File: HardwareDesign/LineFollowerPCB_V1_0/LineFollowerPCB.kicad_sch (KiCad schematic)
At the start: 16 parts, among them J1 B2B-XH-A, J2 B4B-XH-A, J3 Conn_01x04, J4 Conn_01x02_Socket, M1 Motor_DC, M2 Motor_DC, U1 Black Pill v2, U2 DRV8833, U3 AMS1117-3.3, U4 SX1308

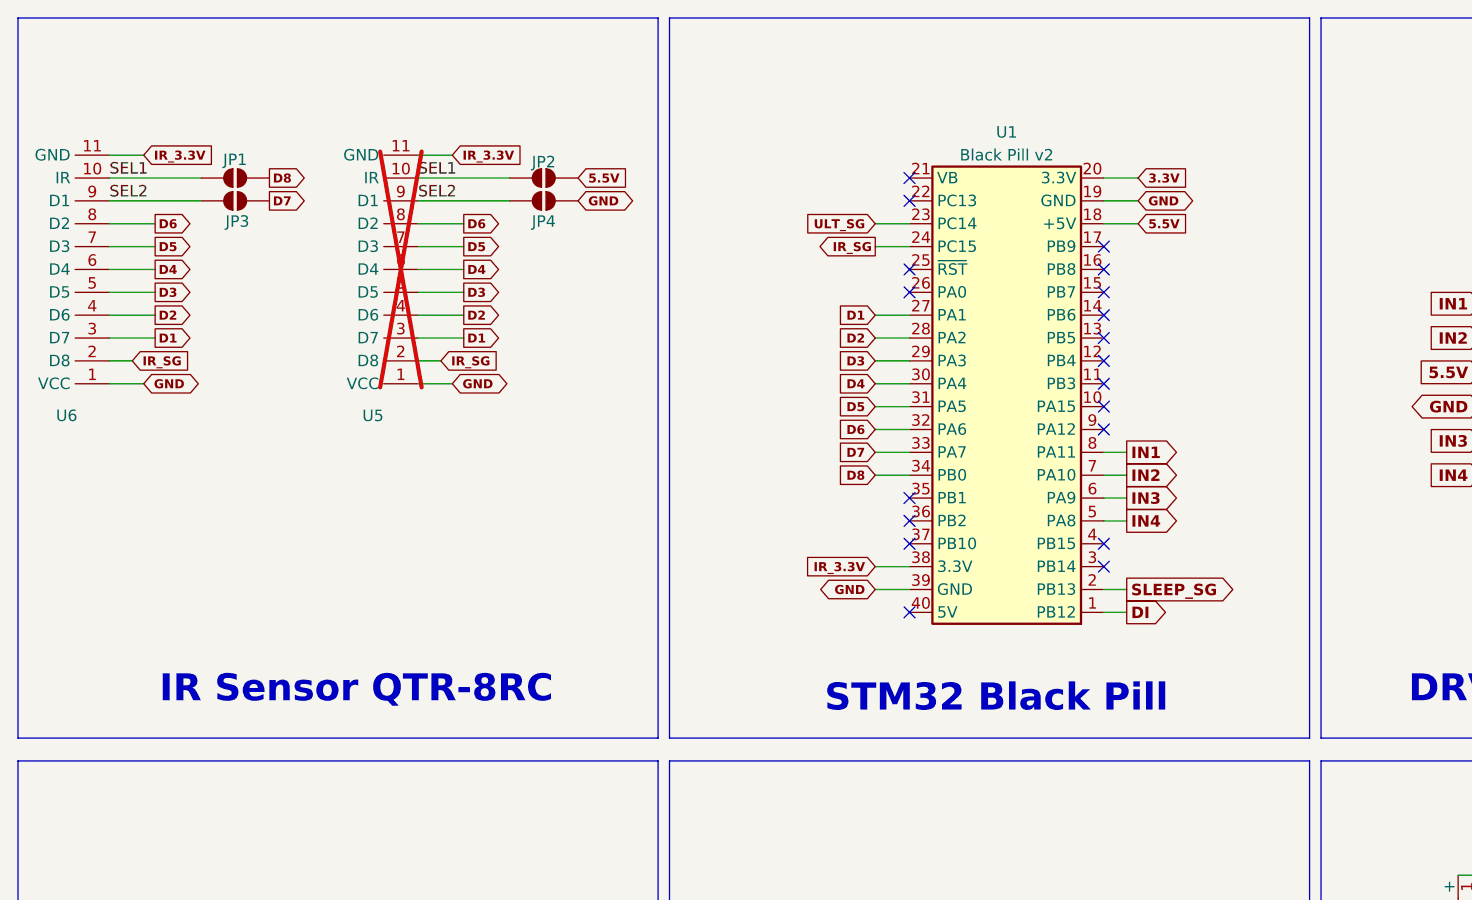
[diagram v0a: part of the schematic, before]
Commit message: Add 1N4001 doide and connect the 5V power signal to the sensor
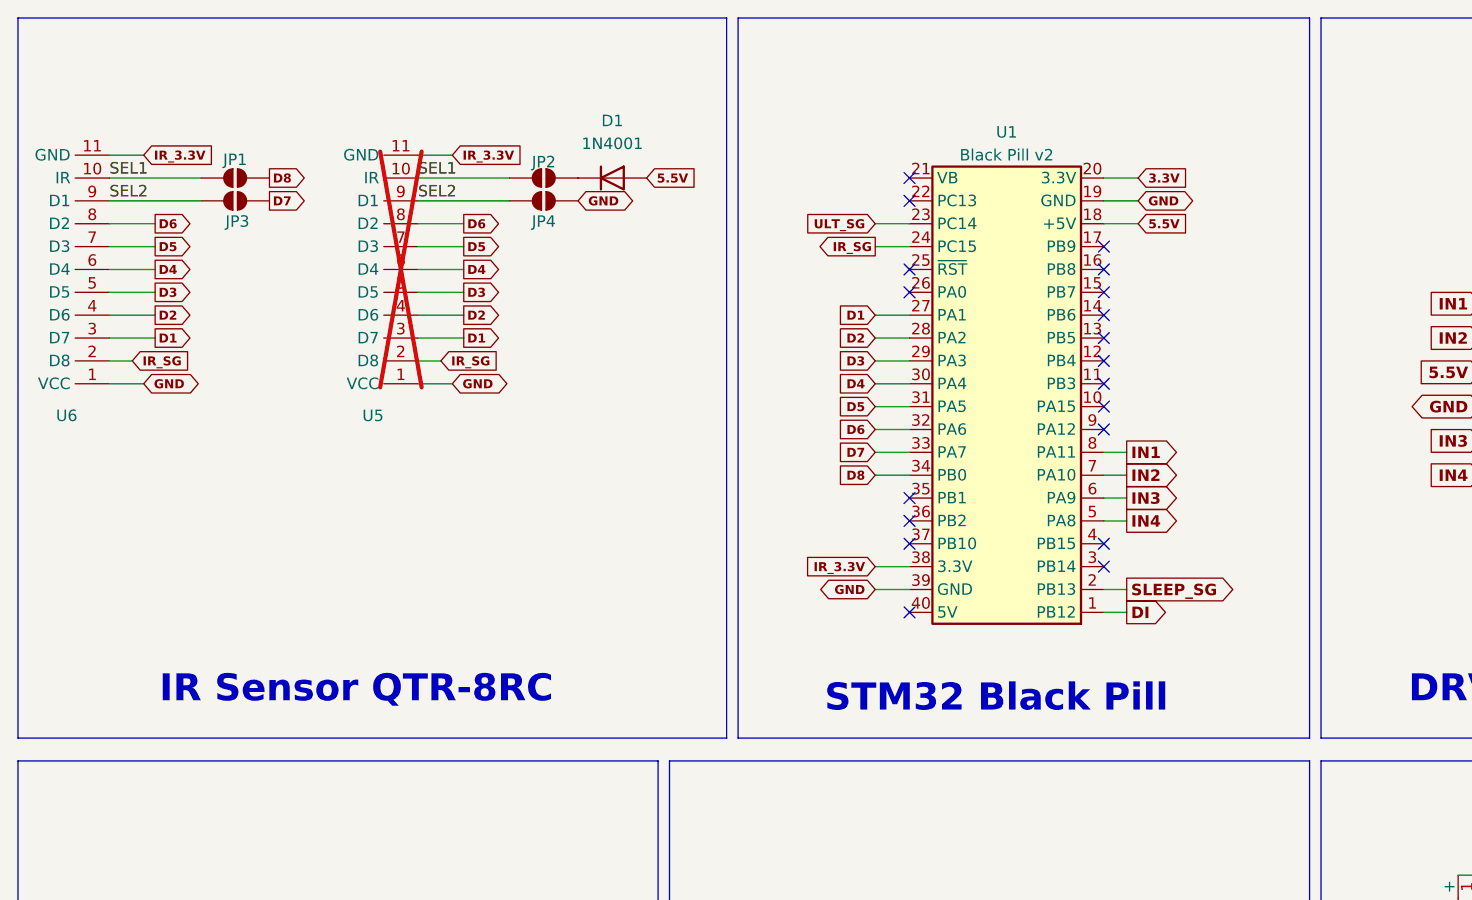
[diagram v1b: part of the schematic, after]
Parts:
- added D1: 1N4001, Diode_THT:D_DO-41_SOD81_P10.16mm_Horizontal, symbol Diode:1N4001
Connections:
- net 5.5V: now also D1.2 (A); no longer JP2.1 (A)
- new net: D1.1 (K), JP2.1 (A)
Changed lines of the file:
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@@
 	)
 	(rectangle
-		(start 85.09 12.7)
+		(start 92.71 12.7)
 		(end 156.21 92.71)
 		(stroke
@@
 	(rectangle
 		(start 12.7 12.7)
-		(end 83.82 92.71)
+		(end 91.44 92.71)
 		(stroke
 			(width 0)
@@
 		)
 	)
+	(global_label "5.5V"
+		(shape input)
+		(at 82.55 30.48 0)
+		(fields_autoplaced yes)
+		(effects
+			(font
+				(size 1 1)
+				(thickness 0.254)
+				(bold yes)
+			)
+			(justify left)
+		)
+		(property "Intersheetrefs" "${INTERSHEET_REFS}"
+			(at 88.7634 30.48 0)
+			(effects
+				(font
+					(size 1.27 1.27)
+				)
+				(justify left)
+				(hide yes)
+			)
+		)
+	)
 	(global_label "GND"
 		(shape bidirectional)
@@
 		)
 	)
-	(global_label "5.5V"
-		(shape input)
-		(at 74.93 30.48 0)
-		(fields_autoplaced yes)
-		(effects
-			(font
-				(size 1 1)
-				(thickness 0.254)
-				(bold yes)
-			)
-			(justify left)
-		)
-		(property "Intersheetrefs" "${INTERSHEET_REFS}"
-			(at 81.1434 30.48 0)
-			(effects
-				(font
-					(size 1.27 1.27)
-				)
-				(justify left)
-				(hide yes)
-			)
-		)
-	)
 	(global_label "OUT1"
 		(shape output)
@@
 					(unit 1)
 				)
+			)
+		)
+	)
+	(symbol
+		(lib_id "Diode:1N4001")
+		(at 78.74 30.48 0)
+		(unit 1)
+		(exclude_from_sim no)
+		(in_bom yes)
+		(on_board yes)
+		(dnp no)
+		(fields_autoplaced yes)
+		(property "Reference" "D1"
+			(at 78.74 24.13 0)
+			(effects
+				(font
+					(size 1.27 1.27)
+				)
+			)
+		)
+		(property "Value" "1N4001"
+			(at 78.74 26.67 0)
+			(effects
+				(font
+					(size 1.27 1.27)
+				)
+			)
+		)
+		(property "Footprint" "Diode_THT:D_DO-41_SOD81_P10.16mm_Horizontal"
+			(at 78.74 30.48 0)
+			(effects
+				(font
+					(size 1.27 1.27)
+				)
+				(hide yes)
+			)
+		)
+		(property "Datasheet" "http://www.vishay.com/docs/88503/1n4001.pdf"
+			(at 78.74 30.48 0)
+			(effects
+				(font
+					(size 1.27 1.27)
+				)
+				(hide yes)
+			)
+		)
+		(property "Description" "50V 1A General Purpose Rectifier Diode, DO-41"
+			(at 78.74 30.48 0)
+			(effects
+				(font
+					(size 1.27 1.27)
+				)
+				(hide yes)
+			)
+		)
+		(property "Sim.Device" "D"
+			(at 78.74 30.48 0)
+			(effects
+				(font
+					(size 1.27 1.27)
+				)
+				(hide yes)
+			)
+		)
+		(property "Sim.Pins" "1=K 2=A"
+			(at 78.74 30.48 0)
+			(effects
+				(font
+					(size 1.27 1.27)
+				)
+				(hide yes)
+			)
+		)
+		(pin "1"
+		)
+		(pin "2"
+		)
+		(instances
+			(project ""
+				(path "/d5afd7c7-15af-4d30-9f5b-830a3ba068cd"
+					(reference "D1")
+					(unit 1)
+				)

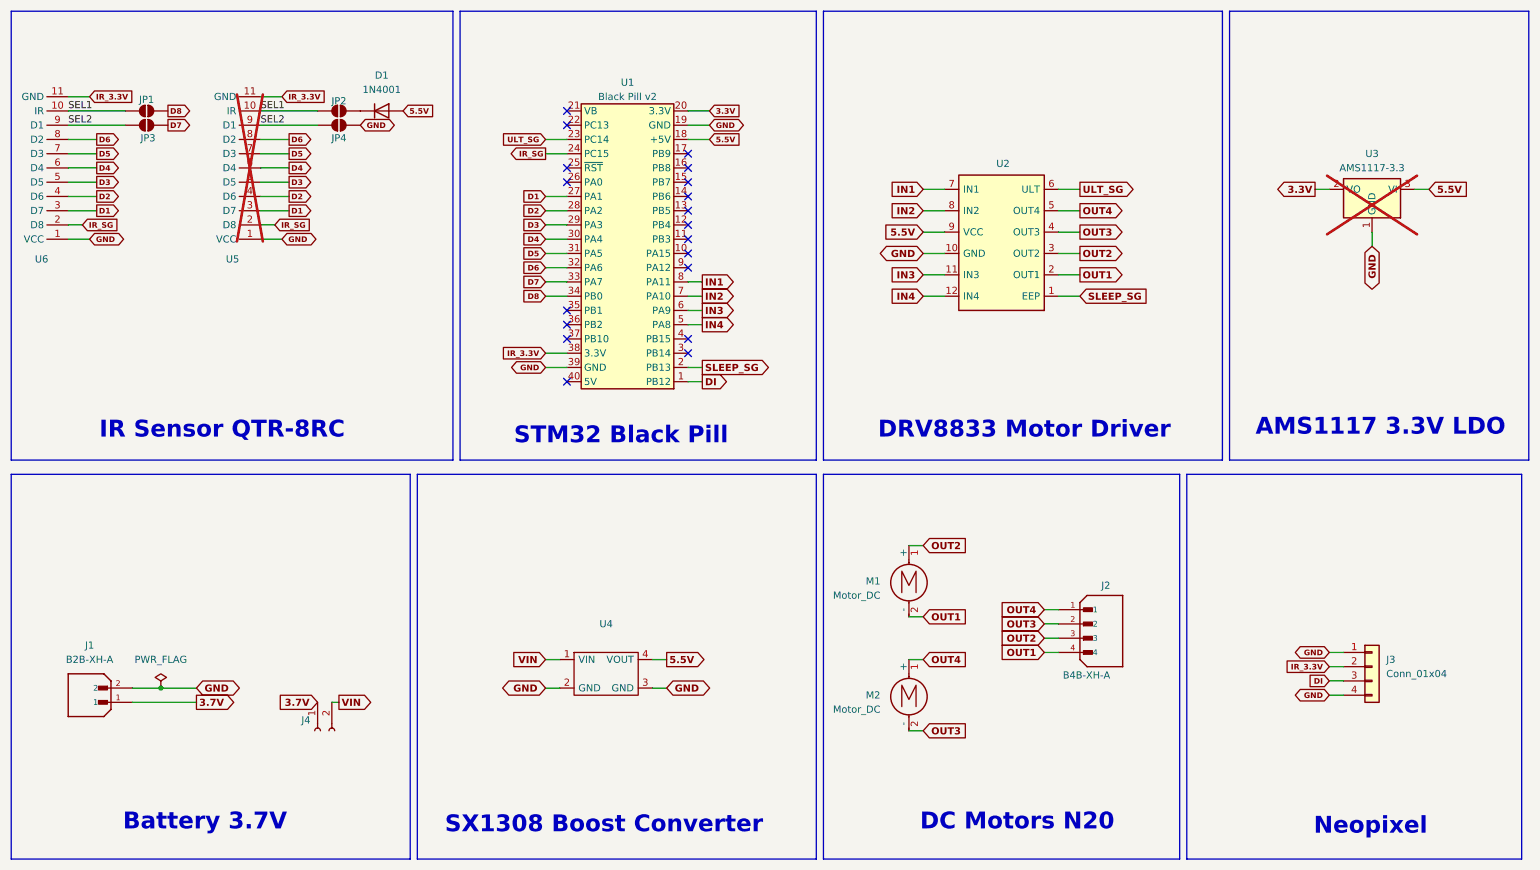
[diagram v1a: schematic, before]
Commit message: Hardware changes: - Change the Neopixel pin to B15 instead of B12 - Add IR pinheader strip - Generate production files
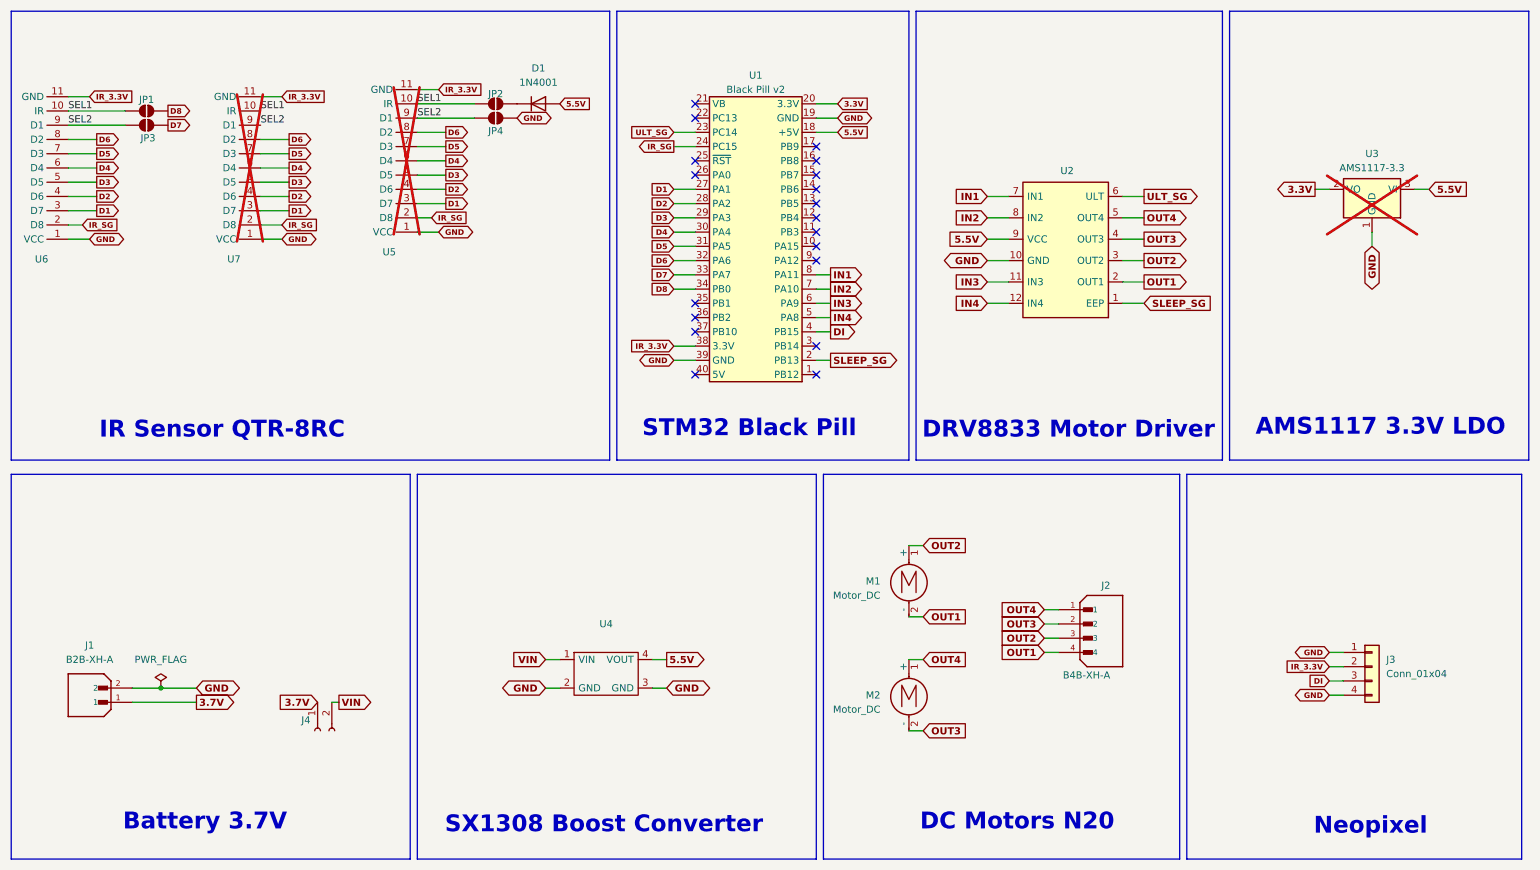
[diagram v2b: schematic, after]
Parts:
- added U7: ~, Connector_PinHeader_2.54mm:PinHeader_1x11_P2.54mm_Vertical, symbol Connector:QTR-8RC
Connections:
- net D1: now also U7.3 (D7)
- net D2: now also U7.4 (D6)
- net D3: now also U7.5 (D5)
- net D4: now also U7.6 (D4)
- net D5: now also U7.7 (D3)
- net D6: now also U7.8 (D2)
- net DI: now also U1.4 (PB15); no longer U1.1 (PB12)
- net GND: now also U7.1 (VCC)
- net IR_3.3V: now also U7.11 (GND)
- net IR_SG: now also U7.2 (D8)
- net SEL1: now also U7.10 (IR)
- net SEL2: now also U7.9 (D1)
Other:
- moved on the sheet: D1, JP2, JP4, U1, U2, U5
